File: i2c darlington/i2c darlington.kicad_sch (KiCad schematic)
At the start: 44 parts, among them IC1 ULN2074B, IC2 ULN2074B, IC3 ULN2074B, IC4 ULN2074B, J1 to qwiic breakout, J2 high current ground, J3 Conn_01x04, J4 Conn_01x04, J5 Conn_01x04, J6 Conn_01x04, J7 Conn_01x01, J8 Conn_01x01, J9 Conn_01x01, U1 PCA9685PW

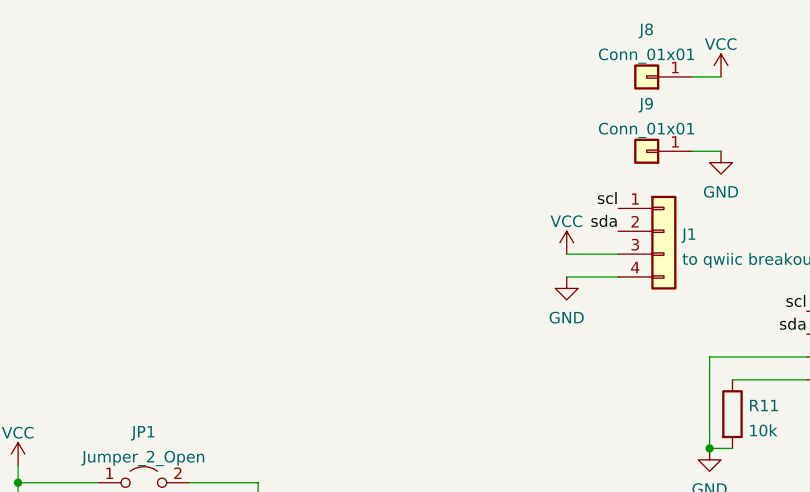
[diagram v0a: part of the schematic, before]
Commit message: added qwiic connectors to boards as well as breakout connector
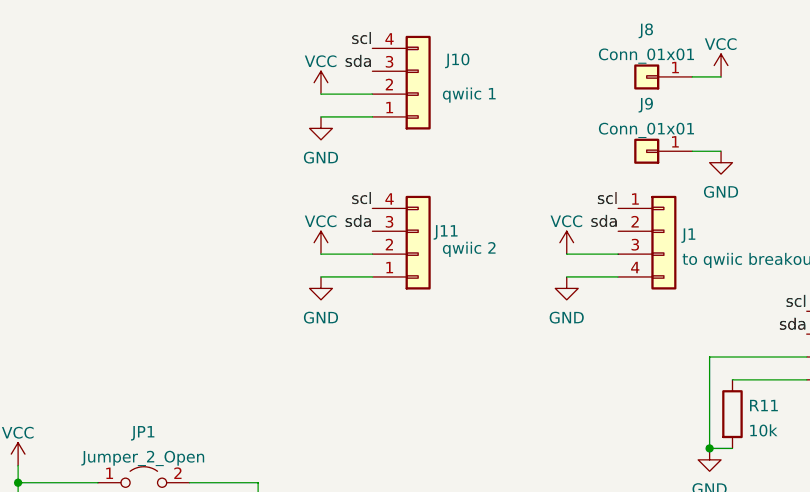
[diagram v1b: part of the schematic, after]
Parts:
- added J10: qwiic 1, Connector_JST:JST_SH_SM04B-SRSS-TB_1x04-1MP_P1.00mm_Horizontal, symbol Connector_Generic:Conn_01x04
- added J11: qwiic 2, Connector_JST:JST_SH_SM04B-SRSS-TB_1x04-1MP_P1.00mm_Horizontal, symbol Connector_Generic:Conn_01x04
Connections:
- net GND: now also J10.1 (Pin_1), J11.1 (Pin_1)
- net VCC: now also J10.2 (Pin_2), J11.2 (Pin_2)
- net scl: now also J10.4 (Pin_4), J11.4 (Pin_4)
- net sda: now also J10.3 (Pin_3), J11.3 (Pin_3)
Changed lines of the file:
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@@
+    (stroke (width 0) (type default) (color 0 0 0 0))
+  )
+  (wire (pts (xy 75.565 41.275) (xy 81.28 41.275))
     (stroke (width 0) (type default) (color 0 0 0 0))
   )
@@
     (stroke (width 0) (type default) (color 0 0 0 0))
   )
+  (wire (pts (xy 75.565 26.035) (xy 81.28 26.035))
+    (stroke (width 0) (type default) (color 0 0 0 0))
+  )
   (wire (pts (xy 96.52 100.965) (xy 96.52 113.665))
     (stroke (width 0) (type default) (color 0 0 0 0))
@@
     (stroke (width 0) (type default) (color 0 0 0 0))
   )
+  (wire (pts (xy 75.565 43.815) (xy 81.28 43.815))
+    (stroke (width 0) (type default) (color 0 0 0 0))
+  )
   (wire (pts (xy 107.95 180.975) (xy 107.95 183.515))
     (stroke (width 0) (type default) (color 0 0 0 0))
@@
   )
   (wire (pts (xy 150.495 168.91) (xy 150.495 173.355))
+    (stroke (width 0) (type default) (color 0 0 0 0))
+  )
+  (wire (pts (xy 75.565 23.495) (xy 81.28 23.495))
     (stroke (width 0) (type default) (color 0 0 0 0))
   )
@@
     (effects (font (size 1.27 1.27)) (justify right bottom))
   )
+  (label "scl" (at 81.28 18.415 180)
+    (effects (font (size 1.27 1.27)) (justify right bottom))
+  )
   (label "pwm4" (at 203.835 95.25 180)
     (effects (font (size 1.27 1.27)) (justify right bottom))
@@
     (effects (font (size 1.27 1.27)) (justify left bottom))
   )
+  (label "scl" (at 81.28 36.195 180)
+    (effects (font (size 1.27 1.27)) (justify right bottom))
+  )
+  (label "sda" (at 81.28 38.735 180)
+    (effects (font (size 1.27 1.27)) (justify right bottom))
+  )
+  (label "sda" (at 81.28 20.955 180)
+    (effects (font (size 1.27 1.27)) (justify right bottom))
+  )
   (label "pwm13" (at 100.33 160.655 180)
     (effects (font (size 1.27 1.27)) (justify right bottom))
@@
     )
     (pin "1")
+  )
+  (symbol (lib_id "Connector_Generic:Conn_01x04") (at 86.36 41.275 0) (mirror x) (unit 1)
+    (in_bom yes) (on_board yes)
+    (property "Reference" "J11" (id 0) (at 89.535 38.735 0))
+    (property "Value" "qwiic 2" (id 1) (at 92.075 40.64 0))
+    (property "Footprint" "Connector_JST:JST_SH_SM04B-SRSS-TB_1x04-1MP_P1.00mm_Horizontal" (id 2) (at 86.36 41.275 0)
+      (effects (font (size 1.27 1.27)) hide)
+    )
+    (property "Datasheet" "~" (id 3) (at 86.36 41.275 0)
+      (effects (font (size 1.27 1.27)) hide)
+    )
+    (pin "1")
+    (pin "2")
+    (pin "3")
+    (pin "4")
   )
   (symbol (lib_id "Connector_Generic:Conn_01x04") (at 264.795 137.795 0) (unit 1)
@@
     (pin "2")
   )
+  (symbol (lib_id "power:GND") (at 75.565 43.815 0) (unit 1)
+    (in_bom yes) (on_board yes) (fields_autoplaced)
+    (property "Reference" "#PWR04" (id 0) (at 75.565 50.165 0)
+      (effects (font (size 1.27 1.27)) hide)
+    )
+    (property "Value" "GND" (id 1) (at 75.565 48.3775 0))
+    (property "Footprint" "" (id 2) (at 75.565 43.815 0)
+      (effects (font (size 1.27 1.27)) hide)
+    )
+    (property "Datasheet" "" (id 3) (at 75.565 43.815 0)
+      (effects (font (size 1.27 1.27)) hide)
+    )
+    (pin "1")
+  )
   (symbol (lib_id "Jumper:Jumper_2_Open") (at 55.88 109.22 0) (unit 1)
     (in_bom yes) (on_board yes) (fields_autoplaced)
@@
     )
     (property "Datasheet" "" (id 3) (at 102.87 43.815 0)
+      (effects (font (size 1.27 1.27)) hide)
+    )
+    (pin "1")
+  )
+  (symbol (lib_id "power:VCC") (at 75.565 23.495 0) (unit 1)
+    (in_bom yes) (on_board yes) (fields_autoplaced)
+    (property "Reference" "#PWR01" (id 0) (at 75.565 27.305 0)
+      (effects (font (size 1.27 1.27)) hide)
+    )
+    (property "Value" "VCC" (id 1) (at 75.565 19.8905 0))
+    (property "Footprint" "" (id 2) (at 75.565 23.495 0)
+      (effects (font (size 1.27 1.27)) hide)
+    )
+    (property "Datasheet" "" (id 3) (at 75.565 23.495 0)
       (effects (font (size 1.27 1.27)) hide)
     )
@@
     (pin "2")
   )
+  (symbol (lib_id "power:GND") (at 75.565 26.035 0) (unit 1)
+    (in_bom yes) (on_board yes) (fields_autoplaced)
+    (property "Reference" "#PWR02" (id 0) (at 75.565 32.385 0)
+      (effects (font (size 1.27 1.27)) hide)
+    )
+    (property "Value" "GND" (id 1) (at 75.565 30.5975 0))
+    (property "Footprint" "" (id 2) (at 75.565 26.035 0)
+      (effects (font (size 1.27 1.27)) hide)
+    )
+    (property "Datasheet" "" (id 3) (at 75.565 26.035 0)
+      (effects (font (size 1.27 1.27)) hide)
+    )
+    (pin "1")
+  )
   (symbol (lib_id "Device:C") (at 133.985 29.21 0) (unit 1)
     (in_bom yes) (on_board yes) (fields_autoplaced)
@@
     (pin "2")
   )
+  (symbol (lib_id "power:VCC") (at 75.565 41.275 0) (unit 1)
+    (in_bom yes) (on_board yes) (fields_autoplaced)
+    (property "Reference" "#PWR03" (id 0) (at 75.565 45.085 0)
+      (effects (font (size 1.27 1.27)) hide)
+    )
+    (property "Value" "VCC" (id 1) (at 75.565 37.6705 0))
+    (property "Footprint" "" (id 2) (at 75.565 41.275 0)
+      (effects (font (size 1.27 1.27)) hide)
+    )
+    (property "Datasheet" "" (id 3) (at 75.565 41.275 0)
+      (effects (font (size 1.27 1.27)) hide)
+    )
+    (pin "1")
+  )
   (symbol (lib_id "Device:R") (at 207.645 80.01 270) (unit 1)
     (in_bom yes) (on_board yes) (fields_autoplaced)
@@
     (pin "1")
   )
+  (symbol (lib_id "Connector_Generic:Conn_01x04") (at 86.36 23.495 0) (mirror x) (unit 1)
+    (in_bom yes) (on_board yes)
+    (property "Reference" "J10" (id 0) (at 90.805 19.685 0))
+    (property "Value" "qwiic 1" (id 1) (at 92.075 23.495 0))
+    (property "Footprint" "Connector_JST:JST_SH_SM04B-SRSS-TB_1x04-1MP_P1.00mm_Horizontal" (id 2) (at 86.36 23.495 0)
+      (effects (font (size 1.27 1.27)) hide)
+    )
+    (property "Datasheet" "~" (id 3) (at 86.36 23.495 0)
+      (effects (font (size 1.27 1.27)) hide)
+    )
+    (pin "1")
+    (pin "2")
+    (pin "3")
+    (pin "4")
+  )
   (symbol (lib_id "power:GND") (at 118.745 62.865 0) (unit 1)
     (in_bom yes) (on_board yes) (fields_autoplaced)
@@
   )
   (symbol_instances
+    (path "/5d42c44e-7087-44c8-a462-56fda612a64e"
+      (reference "#PWR01") (unit 1) (value "VCC") (footprint "")
+    )
+    (path "/b02518ce-d589-4136-8d92-6a2f003b9fa4"
+      (reference "#PWR02") (unit 1) (value "GND") (footprint "")
+    )
+    (path "/befd3fa6-6067-4ccc-9042-262ea69f7846"
+      (reference "#PWR03") (unit 1) (value "VCC") (footprint "")
+    )
+    (path "/2ce5d45c-e9fa-486b-af3e-41fd615fcca1"
+      (reference "#PWR04") (unit 1) (value "GND") (footprint "")
+    )
     (path "/65ee33e1-4dcb-43e8-97a4-10d81d3b60fb"
       (reference "#PWR0101") (unit 1) (value "GND") (footprint "")
@@
       (reference "J9") (unit 1) (value "Conn_01x01") (footprint "Connector_PinHeader_2.54mm:PinHeader_1x01_P2.54mm_Vertical")
     )
+    (path "/f95d2522-b8cf-4bad-9274-e2ae6675619c"
+      (reference "J10") (unit 1) (value "qwiic 1") (footprint "Connector_JST:JST_SH_SM04B-SRSS-TB_1x04-1MP_P1.00mm_Horizontal")
+    )
+    (path "/05fc8d84-967c-4987-b27d-cf145f2617b6"
+      (reference "J11") (unit 1) (value "qwiic 2") (footprint "Connector_JST:JST_SH_SM04B-SRSS-TB_1x04-1MP_P1.00mm_Horizontal")
+    )
     (path "/a1c1ef55-8697-44de-bc64-b151aba7af07"
